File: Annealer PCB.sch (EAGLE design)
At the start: 34 parts

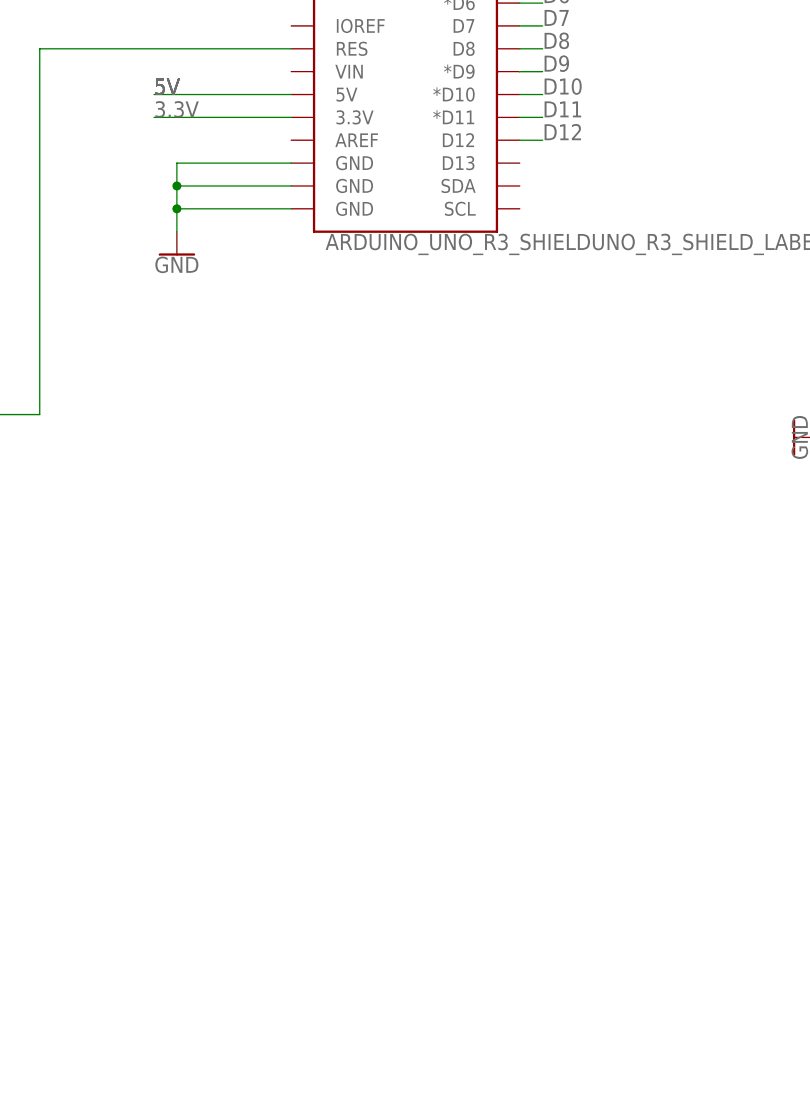
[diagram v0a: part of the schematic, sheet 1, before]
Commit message: Added I2C for an LCD or similar
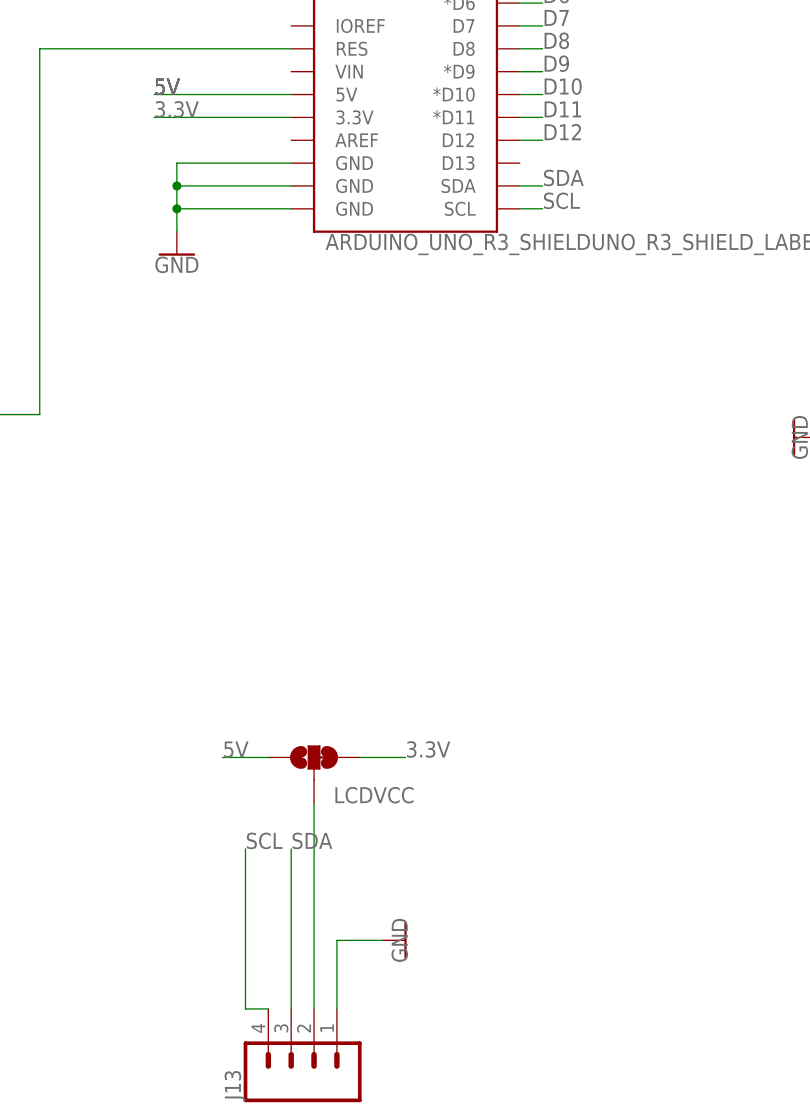
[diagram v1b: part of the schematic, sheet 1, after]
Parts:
- added J13: (no value), SparkFun-Connectors:CONN_04POLAR
- added LCDVCC: JUMPER-SMT_3_1-NC_TRACE_SILK, SparkFun-Jumpers:JUMPER-SMT_3_1-NC_TRACE_SILK
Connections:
- new net N$12: J13.2, LCDVCC.2
- new net SCL: B2.SCL, J13.4
- new net SDA: B2.SDA, J13.3
- net 3.3V: now also LCDVCC.3
- net 5V: now also LCDVCC.1
- net GND: now also J13.1
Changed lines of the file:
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@@
 <part name="J12" library="SparkFun-Connectors" deviceset="CONN_04" device="POLAR"/>
 <part name="GND10" library="SparkFun-PowerSymbols" deviceset="GND" device=""/>
+<part name="J13" library="SparkFun-Connectors" deviceset="CONN_04" device="POLAR"/>
+<part name="GND17" library="SparkFun-PowerSymbols" deviceset="GND" device=""/>
+<part name="LCDVCC" library="SparkFun-Jumpers" deviceset="JUMPER-SMT_3_1-NC_TRACE" device="_SILK" package3d_urn="urn:adsk.eagle:package:39288/1"/>
 </parts>
 <sheets>
@@
 <attribute name="VALUE" x="-44.45" y="86.106" size="1.778" layer="96" font="vector" align="top-left"/>
 </instance>
+<instance part="J13" gate="J1" x="-45.72" y="-5.08" smashed="yes" rot="R90">
+<attribute name="VALUE" x="-38.354" y="-10.16" size="1.778" layer="96" font="vector" rot="R90"/>
+<attribute name="NAME" x="-53.848" y="-10.16" size="1.778" layer="95" font="vector" rot="R90"/>
+</instance>
+<instance part="GND17" gate="1" x="-35.56" y="7.62" smashed="yes" rot="R90">
+<attribute name="VALUE" x="-35.306" y="7.62" size="1.778" layer="96" rot="R270" align="top-center"/>
+</instance>
+<instance part="LCDVCC" gate="G$1" x="-45.72" y="27.94" smashed="yes" rot="R90">
+<attribute name="NAME" x="-43.561" y="22.86" size="1.778" layer="95" font="vector"/>
+</instance>
 </instances>
 <busses>
@@
 <junction x="182.88" y="71.12"/>
 </segment>
+<segment>
+<pinref part="J13" gate="J1" pin="1"/>
+<wire x1="-43.18" y1="0" x2="-43.18" y2="7.62" width="0.1524" layer="91"/>
+<pinref part="GND17" gate="1" pin="GND"/>
+<wire x1="-43.18" y1="7.62" x2="-38.1" y2="7.62" width="0.1524" layer="91"/>
+</segment>
 </net>
 <net name="3.3V" class="0">
@@
 <label x="-63.5" y="99.06" size="1.778" layer="95"/>
 <pinref part="B2" gate="G$1" pin="3.3V"/>
+</segment>
+<segment>
+<pinref part="LCDVCC" gate="G$1" pin="3"/>
+<wire x1="-40.64" y1="27.94" x2="-35.56" y2="27.94" width="0.1524" layer="91"/>
+<label x="-35.56" y="27.94" size="1.778" layer="95"/>
 </segment>
 </net>
@@
 <junction x="190.5" y="93.98"/>
 <label x="193.04" y="109.22" size="1.778" layer="95"/>
+</segment>
+<segment>
+<pinref part="LCDVCC" gate="G$1" pin="1"/>
+<wire x1="-50.8" y1="27.94" x2="-55.88" y2="27.94" width="0.1524" layer="91"/>
+<label x="-55.88" y="27.94" size="1.778" layer="95"/>
 </segment>
 </net>
@@
 </segment>
 </net>
+<net name="SDA" class="0">
+<segment>
+<pinref part="B2" gate="G$1" pin="SDA"/>
+<wire x1="-22.86" y1="91.44" x2="-20.32" y2="91.44" width="0.1524" layer="91"/>
+<label x="-20.32" y="91.44" size="1.778" layer="95"/>
+</segment>
+<segment>
+<pinref part="J13" gate="J1" pin="3"/>
+<wire x1="-48.26" y1="0" x2="-48.26" y2="17.78" width="0.1524" layer="91"/>
+<label x="-48.26" y="17.78" size="1.778" layer="95"/>
+</segment>
+</net>
+<net name="SCL" class="0">
+<segment>
+<pinref part="B2" gate="G$1" pin="SCL"/>
+<wire x1="-22.86" y1="88.9" x2="-20.32" y2="88.9" width="0.1524" layer="91"/>
+<label x="-20.32" y="88.9" size="1.778" layer="95"/>
+</segment>
+<segment>
+<pinref part="J13" gate="J1" pin="4"/>
+<wire x1="-50.8" y1="0" x2="-53.34" y2="0" width="0.1524" layer="91"/>
+<wire x1="-53.34" y1="0" x2="-53.34" y2="17.78" width="0.1524" layer="91"/>
+<label x="-53.34" y="17.78" size="1.778" layer="95"/>
+</segment>
+</net>
+<net name="N$12" class="0">
+<segment>
+<pinref part="J13" gate="J1" pin="2"/>
+<pinref part="LCDVCC" gate="G$1" pin="2"/>
+<wire x1="-45.72" y1="0" x2="-45.72" y2="22.86" width="0.1524" layer="91"/>
+</segment>
+</net>

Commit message: Swap pins on thermistor2 and prox2
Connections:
- net A3: now also J3.1, R4.1; no longer J5.1, R7.1
- net A4: now also J5.1, R7.1; no longer J3.1, R4.1
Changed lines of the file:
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@@
 <pinref part="B2" gate="G$1" pin="A3"/>
 </segment>
-</net>
-<net name="N$2" class="0">
-<segment>
-<pinref part="J2" gate="J$1" pin="3"/>
-<wire x1="88.9" y1="55.88" x2="88.9" y2="58.42" width="0.1524" layer="91"/>
-<wire x1="88.9" y1="58.42" x2="78.74" y2="58.42" width="0.1524" layer="91"/>
-<pinref part="CUR-BYPASS" gate="G$1" pin="2"/>
-<wire x1="78.74" y1="58.42" x2="78.74" y2="60.96" width="0.1524" layer="91"/>
-</segment>
-</net>
-<net name="N$3" class="0">
-<segment>
-<pinref part="R2" gate="G$1" pin="2"/>
-<wire x1="83.82" y1="78.74" x2="76.2" y2="78.74" width="0.1524" layer="91"/>
-<pinref part="CUR-BYPASS" gate="G$1" pin="3"/>
-<wire x1="83.82" y1="78.74" x2="83.82" y2="66.04" width="0.1524" layer="91"/>
-</segment>
-</net>
-<net name="N$4" class="0">
-<segment>
-<pinref part="VOL-BYPASS" gate="G$1" pin="3"/>
-<pinref part="VR1" gate="G$1" pin="1"/>
-<wire x1="27.94" y1="76.2" x2="35.56" y2="83.82" width="0.1524" layer="91"/>
-</segment>
-</net>
-<net name="N$5" class="0">
-<segment>
-<pinref part="J1" gate="G$1" pin="1"/>
-<pinref part="VOL-BYPASS" gate="G$1" pin="2"/>
-<wire x1="22.86" y1="63.5" x2="22.86" y2="71.12" width="0.1524" layer="91"/>
-</segment>
-</net>
-<net name="N$6" class="0">
-<segment>
-<pinref part="R11" gate="G$1" pin="1"/>
-<pinref part="J10" gate="J1" pin="3"/>
-<wire x1="180.34" y1="78.74" x2="185.42" y2="78.74" width="0.1524" layer="91"/>
-<wire x1="185.42" y1="78.74" x2="185.42" y2="58.42" width="0.1524" layer="91"/>
-</segment>
-</net>
-<net name="A4" class="0">
 <segment>
 <pinref part="R4" gate="G$1" pin="1"/>
@@
 <label x="149.86" y="71.12" size="1.778" layer="95"/>
 </segment>
+</net>
+<net name="N$2" class="0">
+<segment>
+<pinref part="J2" gate="J$1" pin="3"/>
+<wire x1="88.9" y1="55.88" x2="88.9" y2="58.42" width="0.1524" layer="91"/>
+<wire x1="88.9" y1="58.42" x2="78.74" y2="58.42" width="0.1524" layer="91"/>
+<pinref part="CUR-BYPASS" gate="G$1" pin="2"/>
+<wire x1="78.74" y1="58.42" x2="78.74" y2="60.96" width="0.1524" layer="91"/>
+</segment>
+</net>
+<net name="N$3" class="0">
+<segment>
+<pinref part="R2" gate="G$1" pin="2"/>
+<wire x1="83.82" y1="78.74" x2="76.2" y2="78.74" width="0.1524" layer="91"/>
+<pinref part="CUR-BYPASS" gate="G$1" pin="3"/>
+<wire x1="83.82" y1="78.74" x2="83.82" y2="66.04" width="0.1524" layer="91"/>
+</segment>
+</net>
+<net name="N$4" class="0">
+<segment>
+<pinref part="VOL-BYPASS" gate="G$1" pin="3"/>
+<pinref part="VR1" gate="G$1" pin="1"/>
+<wire x1="27.94" y1="76.2" x2="35.56" y2="83.82" width="0.1524" layer="91"/>
+</segment>
+</net>
+<net name="N$5" class="0">
+<segment>
+<pinref part="J1" gate="G$1" pin="1"/>
+<pinref part="VOL-BYPASS" gate="G$1" pin="2"/>
+<wire x1="22.86" y1="63.5" x2="22.86" y2="71.12" width="0.1524" layer="91"/>
+</segment>
+</net>
+<net name="N$6" class="0">
+<segment>
+<pinref part="R11" gate="G$1" pin="1"/>
+<pinref part="J10" gate="J1" pin="3"/>
+<wire x1="180.34" y1="78.74" x2="185.42" y2="78.74" width="0.1524" layer="91"/>
+<wire x1="185.42" y1="78.74" x2="185.42" y2="58.42" width="0.1524" layer="91"/>
+</segment>
+</net>
+<net name="A4" class="0">
 <segment>
 <wire x1="-48.26" y1="119.38" x2="-55.88" y2="119.38" width="0.1524" layer="91"/>
@@
 </segment>
 </net>
-<net name="A3" class="0">
-<segment>
-<wire x1="-60.96" y1="40.64" x2="-60.96" y2="30.48" width="0.1524" layer="91"/>
-<wire x1="-60.96" y1="40.64" x2="-43.18" y2="40.64" width="0.1524" layer="91"/>
-<junction x="-60.96" y="40.64"/>
-<label x="-43.18" y="40.64" size="1.778" layer="95"/>
-<pinref part="R7" gate="G$1" pin="1"/>
-<pinref part="J5" gate="G$1" pin="1"/>
-</segment>
-</net>
 <net name="D4" class="0">
 <segment>
@@
 </segment>
 </net>
+<net name="A4" class="0">
+<segment>
+<wire x1="-60.96" y1="40.64" x2="-60.96" y2="30.48" width="0.1524" layer="91"/>
+<wire x1="-60.96" y1="40.64" x2="-43.18" y2="40.64" width="0.1524" layer="91"/>
+<junction x="-60.96" y="40.64"/>
+<label x="-43.18" y="40.64" size="1.778" layer="95"/>
+<pinref part="R7" gate="G$1" pin="1"/>
+<pinref part="J5" gate="G$1" pin="1"/>
+</segment>
+</net>
